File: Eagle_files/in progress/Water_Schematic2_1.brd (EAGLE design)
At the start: 26.4 x 45.5 mm, 10 parts

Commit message: updating readme
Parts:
- moved POT2 1.48 mm to (7.87, 21.6)
- moved POT1 0.92 mm to (7.87, 14.2)
- moved R1 0.25 mm to (13.7, 26.9)
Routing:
- net VCC: track 81.0 -> 82.7 mm
- net A6: track 4.40 -> 5.67 mm
- net GND: track 111.0 -> 111.8 mm
- net A7: track 5.84 -> 5.33 mm
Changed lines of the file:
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@@
 </autorouter>
 <elements>
-<element name="R1" library="rcl" library_urn="urn:adsk.eagle:library:334" package="0204/7" package3d_urn="urn:adsk.eagle:package:23498/2" value="4.7K" x="13.716" y="26.67" smashed="yes" rot="R90">
-<attribute name="NAME" x="17.399" y="24.765" size="1.27" layer="25" ratio="10" rot="R90"/>
-<attribute name="POPULARITY" value="48" x="63.246" y="67.31" size="1.778" layer="27" rot="R90" display="off"/>
-<attribute name="SPICEPREFIX" value="R" x="63.246" y="67.31" size="1.778" layer="27" rot="R90" display="off"/>
-<attribute name="VALUE" x="14.4018" y="24.384" size="1.27" layer="27" ratio="10" rot="R90"/>
+<element name="R1" library="rcl" library_urn="urn:adsk.eagle:library:334" package="0204/7" package3d_urn="urn:adsk.eagle:package:23498/2" value="4.7K" x="13.716" y="26.924" smashed="yes" rot="R90">
+<attribute name="NAME" x="17.399" y="25.019" size="1.27" layer="25" ratio="10" rot="R90"/>
+<attribute name="POPULARITY" value="48" x="63.246" y="67.564" size="1.778" layer="27" rot="R90" display="off"/>
+<attribute name="SPICEPREFIX" value="R" x="63.246" y="67.564" size="1.778" layer="27" rot="R90" display="off"/>
+<attribute name="VALUE" x="14.4018" y="24.638" size="1.27" layer="27" ratio="10" rot="R90"/>
 </element>
 <element name="ARDUINO" library="SparkFun-Boards" library_urn="urn:adsk.eagle:library:509" package="ARDUINO_PRO_MINI" package3d_urn="urn:adsk.eagle:package:37322/1" value="ARDUINO_PRO_MINI" x="11.176" y="23.368" smashed="yes">
@@
 <attribute name="VALUE" x="2.286" y="40.132" size="0.6096" layer="27" font="vector" ratio="20" align="top-left"/>
 </element>
-<element name="POT1" library="RM_065" package="RM_065" value="RM_065" x="8.636" y="14.732" smashed="yes" rot="R270"/>
-<element name="POT2" library="RM_065" package="RM_065" value="RM_065" x="8.636" y="22.86" smashed="yes" rot="R270"/>
+<element name="POT1" library="RM_065" package="RM_065" value="RM_065" x="7.874" y="14.224" smashed="yes" rot="R270"/>
+<element name="POT2" library="RM_065" package="RM_065" value="RM_065" x="7.874" y="21.59" smashed="yes" rot="R270"/>
 </elements>
 <signals>
@@
 <wire x1="23.622" y1="5.08" x2="21.59" y2="5.08" width="0.508" layer="16"/>
 <wire x1="21.59" y1="5.08" x2="21.59" y2="18.11879375" width="0.508" layer="16"/>
-<wire x1="13.716" y1="22.86" x2="17.018" y2="22.86" width="0.508" layer="16"/>
-<wire x1="17.018" y1="22.86" x2="17.018" y2="18.288" width="0.508" layer="16"/>
+<wire x1="13.716" y1="23.114" x2="17.018" y2="23.114" width="0.508" layer="16"/>
+<wire x1="17.018" y1="23.114" x2="17.018" y2="18.288" width="0.508" layer="16"/>
 <wire x1="17.018" y1="18.288" x2="18.796" y2="18.288" width="0.508" layer="16"/>
 </signal>
@@
 <wire x1="3.556" y1="28.448" x2="1.778" y2="28.448" width="0.508" layer="16"/>
 <wire x1="5.31719375" y1="36.9316" x2="5.2324" y2="36.84680625" width="0.508" layer="16"/>
-<wire x1="5.2324" y1="26.416" x2="6.096" y2="26.416" width="0.508" layer="16"/>
-<wire x1="6.096" y1="26.416" x2="8.382" y2="26.416" width="0.508" layer="16"/>
+<wire x1="5.334" y1="26.416" x2="8.382" y2="26.416" width="0.508" layer="16"/>
 <wire x1="5.2324" y1="36.84680625" x2="5.2324" y2="28.448" width="0.508" layer="16"/>
-<wire x1="5.2324" y1="28.448" x2="5.2324" y2="26.416" width="0.508" layer="16"/>
+<wire x1="5.334" y1="28.448" x2="5.334" y2="26.416" width="0.508" layer="16"/>
 <wire x1="3.556" y1="28.448" x2="5.2324" y2="28.448" width="0.508" layer="16"/>
-<wire x1="6.096" y1="4.826" x2="6.096" y2="14.732" width="0.508" layer="16"/>
-<wire x1="6.096" y1="14.732" x2="6.096" y2="22.86" width="0.508" layer="16"/>
-<wire x1="6.096" y1="22.86" x2="6.096" y2="26.416" width="0.508" layer="16"/>
-<wire x1="8.636" y1="22.86" x2="6.096" y2="22.86" width="0.508" layer="16"/>
-<wire x1="8.636" y1="14.732" x2="6.096" y2="14.732" width="0.508" layer="16"/>
+<wire x1="5.2324" y1="28.448" x2="5.334" y2="28.448" width="0.508" layer="16"/>
+<wire x1="5.334" y1="14.224" x2="5.334" y2="4.826" width="0.508" layer="16"/>
+<wire x1="6.096" y1="4.826" x2="5.334" y2="4.826" width="0.508" layer="16"/>
+<wire x1="5.334" y1="14.224" x2="5.334" y2="21.59" width="0.508" layer="16"/>
+<wire x1="5.334" y1="21.59" x2="5.334" y2="26.416" width="0.508" layer="16"/>
+<wire x1="7.874" y1="21.59" x2="5.334" y2="21.59" width="0.508" layer="16"/>
+<wire x1="7.874" y1="14.224" x2="5.334" y2="14.224" width="0.508" layer="16"/>
 <wire x1="18.796" y1="33.528" x2="19.304" y2="33.528" width="0" layer="19" extent="16-16"/>
 </signal>
@@
 <contactref element="TEMP" pad="3"/>
 <contactref element="RTC" pad="2"/>
-<wire x1="17.2212" y1="30.226" x2="13.97" y2="30.226" width="0.508" layer="16"/>
-<wire x1="13.716" y1="30.48" x2="13.97" y2="30.226" width="0.508" layer="16"/>
+<wire x1="17.2212" y1="30.226" x2="14.224" y2="30.226" width="0.508" layer="16"/>
+<wire x1="13.716" y1="30.734" x2="14.224" y2="30.226" width="0.508" layer="16"/>
 <wire x1="8.636" y1="1.8288" x2="8.636" y2="4.826" width="0.508" layer="16"/>
 <contactref element="POT2" pad="VCC"/>
 <contactref element="POT1" pad="VCC"/>
-<wire x1="13.716" y1="30.48" x2="13.716" y2="36.0172" width="0.508" layer="16"/>
+<wire x1="13.716" y1="30.734" x2="13.716" y2="36.0172" width="0.508" layer="16"/>
 <wire x1="13.716" y1="36.0172" x2="6.1468" y2="36.0172" width="0.508" layer="16"/>
 <wire x1="6.1468" y1="28.92200625" x2="6.1468" y2="36.0172" width="0.508" layer="16"/>
@@
 <wire x1="17.2212" y1="28.448" x2="18.796" y2="28.448" width="0.508" layer="16"/>
 <wire x1="22.86" y1="28.448" x2="18.796" y2="28.448" width="0.508" layer="16"/>
-<wire x1="8.636" y1="9.7536" x2="10.16" y2="9.7536" width="0.508" layer="16"/>
-<wire x1="10.16" y1="9.7536" x2="10.16" y2="17.8816" width="0.508" layer="16"/>
-<wire x1="8.636" y1="4.826" x2="8.636" y2="9.7536" width="0.508" layer="16"/>
-<wire x1="10.16" y1="17.8816" x2="8.636" y2="17.8816" width="0.508" layer="16"/>
-<wire x1="10.16" y1="28.956" x2="10.16" y2="17.8816" width="0.508" layer="16"/>
+<wire x1="7.874" y1="9.2456" x2="10.16" y2="9.2456" width="0.508" layer="16"/>
+<wire x1="10.16" y1="9.2456" x2="10.16" y2="16.6116" width="0.508" layer="16"/>
+<wire x1="7.874" y1="9.2456" x2="7.874" y2="5.588" width="0.508" layer="16"/>
+<wire x1="8.636" y1="4.826" x2="7.874" y2="5.588" width="0.508" layer="16"/>
+<wire x1="10.16" y1="16.6116" x2="7.874" y2="16.6116" width="0.508" layer="16"/>
+<wire x1="10.16" y1="28.956" x2="10.16" y2="16.6116" width="0.508" layer="16"/>
 </signal>
 <signal name="SDA">
@@
 <contactref element="ARDUINO" pad="A6"/>
 <contactref element="POT1" pad="OUT"/>
-<wire x1="15.9385" y1="14.31925" x2="13.6144" y2="14.31925" width="0.508" layer="16"/>
-<wire x1="13.6144" y1="14.31925" x2="13.6144" y2="12.2428" width="0.508" layer="16"/>
+<wire x1="15.9385" y1="14.31925" x2="12.8524" y2="14.31925" width="0.508" layer="16"/>
+<wire x1="12.8524" y1="14.31925" x2="12.8524" y2="11.7348" width="0.508" layer="16"/>
 </signal>
 <signal name="A7">
 <contactref element="ARDUINO" pad="A7"/>
 <contactref element="POT2" pad="OUT"/>
-<wire x1="15.9385" y1="16.85925" x2="15.9385" y2="20.3708" width="0.508" layer="16"/>
-<wire x1="15.9385" y1="20.3708" x2="13.6144" y2="20.3708" width="0.508" layer="16"/>
+<wire x1="15.9385" y1="16.85925" x2="15.9385" y2="19.1008" width="0.508" layer="16"/>
+<wire x1="15.9385" y1="19.1008" x2="12.8524" y2="19.1008" width="0.508" layer="16"/>
 </signal>
 </signals>

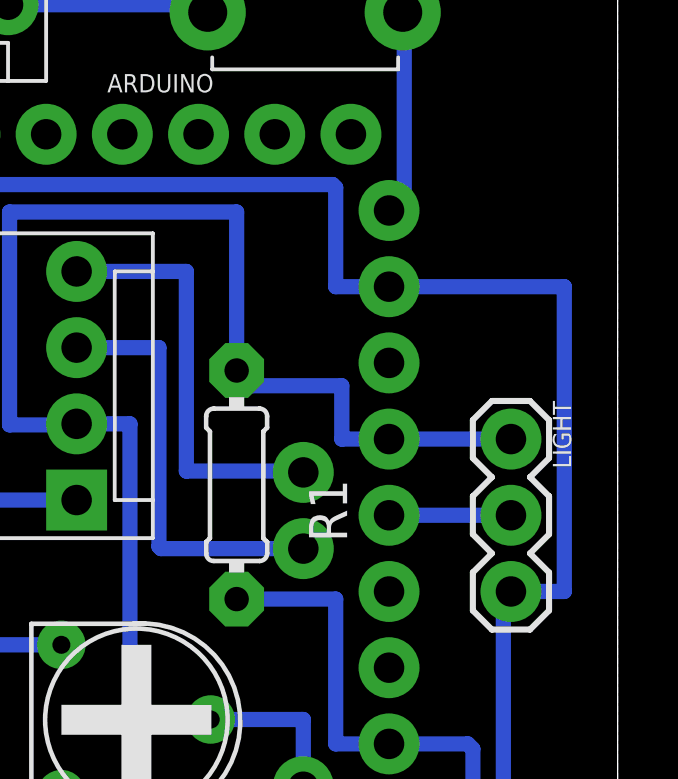
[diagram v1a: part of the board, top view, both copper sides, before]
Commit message: Removing unnecessary files; minor tweaks to board and schematic, like removing value from pots
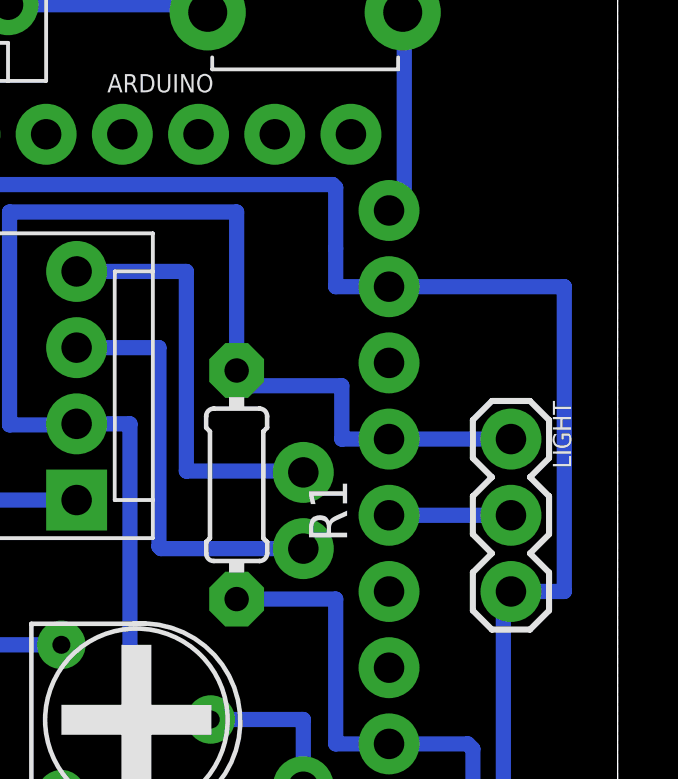
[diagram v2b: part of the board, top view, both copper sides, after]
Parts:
- POT1, POT2: value RM_065 -> (none)
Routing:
- net GND: track 111.8 -> 112.3 mm
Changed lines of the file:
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@@
 <attribute name="VALUE" x="2.286" y="40.132" size="0.6096" layer="27" font="vector" ratio="20" align="top-left"/>
 </element>
-<element name="POT1" library="RM_065" package="RM_065" value="RM_065" x="7.874" y="14.224" smashed="yes" rot="R270"/>
-<element name="POT2" library="RM_065" package="RM_065" value="RM_065" x="7.874" y="21.59" smashed="yes" rot="R270"/>
+<element name="POT1" library="RM_065" package="RM_065" value="" x="7.874" y="14.224" smashed="yes" rot="R270"/>
+<element name="POT2" library="RM_065" package="RM_065" value="" x="7.874" y="21.59" smashed="yes" rot="R270"/>
 </elements>
 <signals>
@@
 <contactref element="POT2" pad="GND"/>
 <wire x1="18.796" y1="33.528" x2="17.018" y2="33.528" width="0.508" layer="16"/>
-<wire x1="17.018" y1="33.528" x2="17.018" y2="36.83" width="0.508" layer="16"/>
+<wire x1="17.018" y1="33.528" x2="17.018" y2="34.798" width="0.508" layer="16"/>
+<wire x1="17.018" y1="34.798" x2="17.018" y2="36.83" width="0.508" layer="16"/>
 <wire x1="17.018" y1="36.83" x2="16.9164" y2="36.9316" width="0.508" layer="16"/>
 <wire x1="16.9164" y1="36.9316" x2="5.31719375" y2="36.9316" width="0.508" layer="16"/>
@@
 <wire x1="22.606" y1="23.114" x2="22.606" y2="7.62" width="0.508" layer="16"/>
 <wire x1="22.606" y1="7.62" x2="23.622" y2="7.62" width="0.508" layer="16"/>
-<wire x1="24.638" y1="23.368" x2="24.638" y2="33.528" width="0.508" layer="16"/>
+<wire x1="24.638" y1="33.528" x2="24.638" y2="23.368" width="0.508" layer="16"/>
 <wire x1="22.86" y1="23.368" x2="24.638" y2="23.368" width="0.508" layer="16"/>
-<wire x1="24.638" y1="33.528" x2="19.304" y2="33.528" width="0.508" layer="16"/>
 <wire x1="3.556" y1="28.448" x2="1.778" y2="28.448" width="0.508" layer="16"/>
 <wire x1="5.31719375" y1="36.9316" x2="5.2324" y2="36.84680625" width="0.508" layer="16"/>
@@
 <wire x1="7.874" y1="21.59" x2="5.334" y2="21.59" width="0.508" layer="16"/>
 <wire x1="7.874" y1="14.224" x2="5.334" y2="14.224" width="0.508" layer="16"/>
-<wire x1="18.796" y1="33.528" x2="19.304" y2="33.528" width="0" layer="19" extent="16-16"/>
+<wire x1="18.796" y1="33.528" x2="24.638" y2="33.528" width="0.508" layer="16"/>
+<wire x1="17.018" y1="34.798" x2="17.018" y2="34.798" width="0.508" layer="16"/>
 </signal>
 <signal name="VCC">
